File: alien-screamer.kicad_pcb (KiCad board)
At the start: 2 copper layers, 34 parts, among them Q2 2N3904, Q3 2N3904, SW1 S4

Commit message: commit
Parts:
- added X1-1: TestPoint, TestPoint:TestPoint_THTPad_D1.0mm_Drill0.5mm, F.Cu at (217.0, 65.5)
- added X13: TestPoint, TestPoint:TestPoint_THTPad_D1.0mm_Drill0.5mm, F.Cu at (166.9, 105.9)
- added X13-1: TestPoint, TestPoint:TestPoint_THTPad_D1.0mm_Drill0.5mm, F.Cu at (238.5, 70.5)
- added X14: TestPoint, TestPoint:TestPoint_THTPad_D1.0mm_Drill0.5mm, F.Cu at (166.9, 112.0)
- added X14-1: TestPoint, TestPoint:TestPoint_THTPad_D1.0mm_Drill0.5mm, F.Cu at (232.0, 69.5)
- added X2: TestPoint, TestPoint:TestPoint_THTPad_D1.0mm_Drill0.5mm, F.Cu at (204.5, 67.0)
- added X2-1: TestPoint, TestPoint:TestPoint_THTPad_D1.0mm_Drill0.5mm, F.Cu at (173.0, 105.9)
- added X3: TestPoint, TestPoint:TestPoint_THTPad_D1.0mm_Drill0.5mm, F.Cu at (224.0, 68.0)
- added X3-1: TestPoint, TestPoint:TestPoint_THTPad_D1.0mm_Drill0.5mm, F.Cu at (173.0, 112.0)
- added X4: TestPoint, TestPoint:TestPoint_THTPad_D1.0mm_Drill0.5mm, F.Cu at (160.8, 105.9)
- added X4-1: TestPoint, TestPoint:TestPoint_THTPad_D1.0mm_Drill0.5mm, F.Cu at (186.5, 66.5)
- added X5: TestPoint, TestPoint:TestPoint_THTPad_D1.0mm_Drill0.5mm, F.Cu at (160.8, 112.0)
- added X5-1: TestPoint, TestPoint:TestPoint_THTPad_D1.0mm_Drill0.5mm, F.Cu at (184.0, 66.5)
- added X6: TestPoint, TestPoint:TestPoint_THTPad_D1.0mm_Drill0.5mm, F.Cu at (221.0, 71.0)
- added X6-1: TestPoint, TestPoint:TestPoint_THTPad_D1.0mm_Drill0.5mm, F.Cu at (179.1, 99.8)
- added X7: TestPoint, TestPoint:TestPoint_THTPad_D1.0mm_Drill0.5mm, F.Cu at (166.9, 93.7)
- added X7-1: TestPoint, TestPoint:TestPoint_THTPad_D1.0mm_Drill0.5mm, F.Cu at (179.1, 105.9)
- added X8: TestPoint, TestPoint:TestPoint_THTPad_D1.0mm_Drill0.5mm, F.Cu at (166.9, 99.8)
- added X9-1: TestPoint, TestPoint:TestPoint_THTPad_D1.0mm_Drill0.5mm, F.Cu at (179.1, 112.0)
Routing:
- net Net-(R4-Pad2): track 0.00 -> 19.8 mm, vias 0 -> 1
- net Net-(C12-Pad1): track 0.00 -> 18.0 mm
- net Net-(Q1-S): track 0.40 -> 17.9 mm
- net Net-(R6-Pad2): track 0.00 -> 14.3 mm
- net Net-(R10-Pad1): track 0.00 -> 13.8 mm
- net Net-(S3-B): track 0.00 -> 10.9 mm
- net Net-(S1-A): track 23.6 -> 31.2 mm
- net Net-(S2-A): track 0.50 -> 8.00 mm

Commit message: commit
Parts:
- added B1: TestPoint_2Pole, TestPoint:TestPoint_2Pads_Pitch5.08mm_Drill1.3mm, F.Cu at (201.6, 104.8)
- added C1: 100p, TestPoint:TestPoint_2Pads_Pitch5.08mm_Drill1.3mm, F.Cu at (201.6, 109.4)
- added C10: 220u, Capacitor_THT:CP_Radial_D10.0mm_P5.00mm, F.Cu at (76.5, 102.0)
- added C11: .1u, Capacitor_THT:C_Disc_D7.5mm_W5.0mm_P5.00mm, F.Cu at (56.9, 107.6)
- added C12: 1u, Capacitor_THT:C_Disc_D7.5mm_W5.0mm_P5.00mm, F.Cu at (65.9, 88.0)
- added C13: .047u, Capacitor_THT:C_Disc_D7.5mm_W5.0mm_P5.00mm, F.Cu at (65.9, 94.5)
- added C14: 10u, Capacitor_THT:C_Disc_D7.5mm_W5.0mm_P5.00mm, F.Cu at (65.9, 101.0)
- added C2: 1u, Capacitor_THT:C_Disc_D7.5mm_W5.0mm_P5.00mm, F.Cu at (47.8, 88.0)
- added C3: .001u, Capacitor_THT:C_Disc_D7.5mm_W5.0mm_P5.00mm, F.Cu at (47.8, 94.5)
- added C4: 1u, Capacitor_THT:C_Disc_D7.5mm_W5.0mm_P5.00mm, F.Cu at (47.8, 101.0)
- added C5: 1u, Capacitor_THT:C_Disc_D7.5mm_W5.0mm_P5.00mm, F.Cu at (47.8, 107.6)
- added C6: .01u, Capacitor_THT:C_Disc_D7.5mm_W5.0mm_P5.00mm, F.Cu at (56.9, 88.0)
- added C7: .1u, Capacitor_THT:C_Disc_D7.5mm_W5.0mm_P5.00mm, F.Cu at (56.9, 94.5)
- added C8: 470u, Capacitor_THT:CP_Radial_D10.0mm_P5.00mm, F.Cu at (76.5, 90.5)
- added C9: .1u, Capacitor_THT:C_Disc_D7.5mm_W5.0mm_P5.00mm, F.Cu at (56.9, 101.0)
- added D1: D, Diode_THT:D_DO-15_P10.16mm_Horizontal, F.Cu at (201.2, 99.9)
- added J1: AudioJack2, TestPoint:TestPoint_2Pads_Pitch5.08mm_Drill1.3mm, F.Cu at (201.6, 114.1)
- added LFO1: LED1, LED_THT:LED_D5.0mm, F.Cu at (211.4, 106.2)
- added Q1: 2N5457, Package_TO_SOT_THT:TO-92_HandSolder, F.Cu at (211.0, 113.5)
- added TP1: TestPoint_2Pole, TestPoint:TestPoint_2Pads_Pitch5.08mm_Drill1.3mm, F.Cu at (59.7, 124.9)
- added U1: LM324, Package_DIP:DIP-14_W7.62mm_LongPads, F.Cu at (47.8, 112.9)
- added U2: LM386, Package_DIP:DIP-8_W7.62mm_LongPads, F.Cu at (59.4, 112.9)
- added X1: TestPoint, TestPoint:TestPoint_THTPad_D1.0mm_Drill0.5mm, F.Cu at (214.9, 98.8)

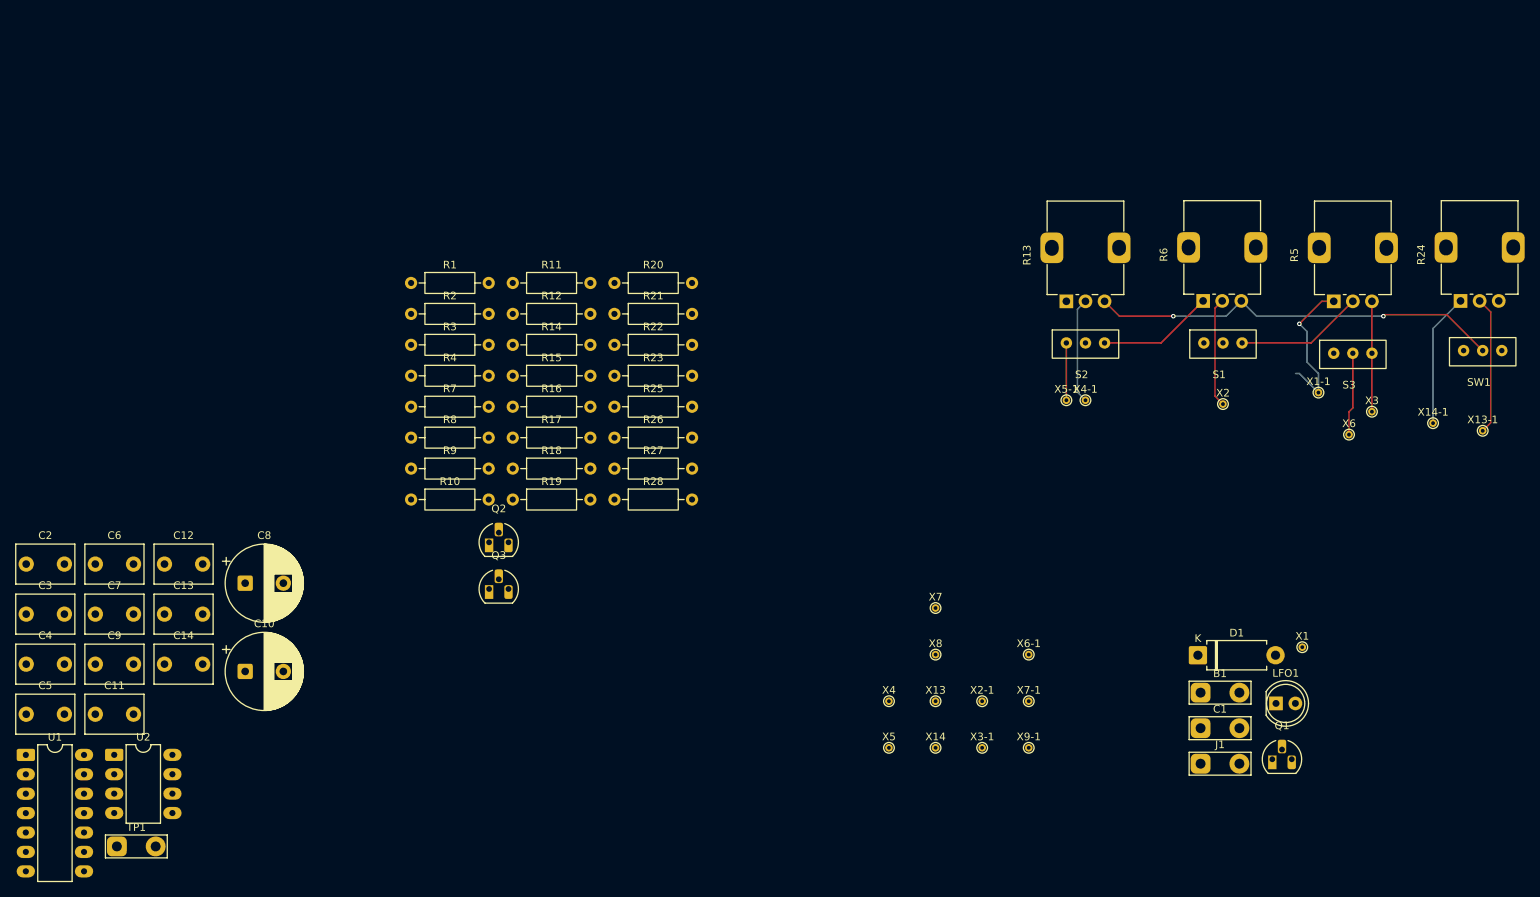
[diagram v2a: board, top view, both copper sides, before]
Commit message: Finished PCB, experimenting with connectors - unsure if it will work but have sent off PCB design for fabrication
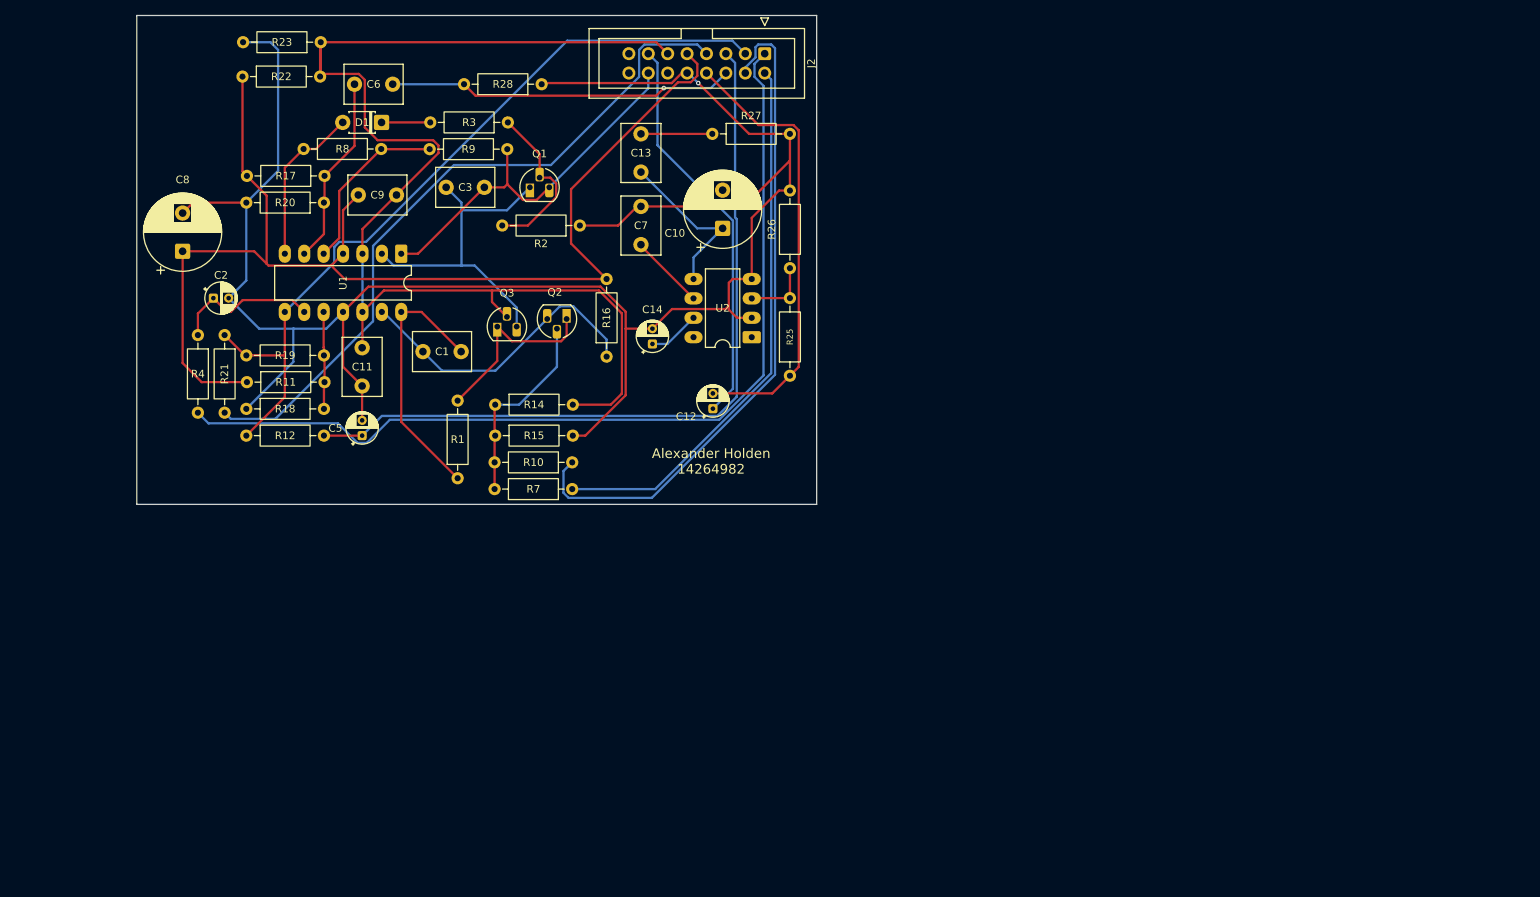
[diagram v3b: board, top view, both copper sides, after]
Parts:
- removed B1, TP1: TestPoint_2Pole, TestPoint:TestPoint_2Pads_Pitch5.08mm_Drill1.3mm
- removed C4: 1u, Capacitor_THT:C_Disc_D7.5mm_W5.0mm_P5.00mm
- removed J1: AudioJack2, TestPoint:TestPoint_2Pads_Pitch5.08mm_Drill1.3mm
- removed LFO1: LED1, LED_THT:LED_D5.0mm
- removed R13, R24, R6: 100K, Potentiometer_THT:Potentiometer_Alps_RK09K_Single_Vertical
- removed R5: 1M, Potentiometer_THT:Potentiometer_Alps_RK09K_Single_Vertical
- removed S1: SW_SPST, PROJECT_FOOTPRINTS:spdt
- removed S2: SW_SPDT_312, PROJECT_FOOTPRINTS:spdt
- removed S3: SYNC, PROJECT_FOOTPRINTS:spdt
- removed SW1: S4, PROJECT_FOOTPRINTS:spdt
- removed X1, X1-1, X13, X13-1, X14, X14-1, X2, X2-1, X3, X3-1, X4, X4-1, X5, X5-1, X6, X6-1, X7, X7-1, X8, X9-1: TestPoint, TestPoint:TestPoint_THTPad_D1.0mm_Drill0.5mm
- added J2: Conn_02x08_Odd_Even, PROJECT_FOOTPRINTS:IDC-Header_2x08_P2.54mm_Vertical, F.Cu at (144.5, 21.1)
- C1: footprint TestPoint:TestPoint_2Pads_Pitch5.08mm_Drill1.3mm -> Capacitor_THT:C_Disc_D7.5mm_W5.0mm_P5.00mm
- C12, C14, C2, C5: footprint Capacitor_THT:C_Disc_D7.5mm_W5.0mm_P5.00mm -> Capacitor_THT:CP_Radial_D4.0mm_P2.00mm
- D1: footprint Diode_THT:D_DO-15_P10.16mm_Horizontal -> Diode_THT:D_T-1_P5.08mm_Horizontal
- moved D1 127.6 mm to (94.3, 30.1), turned to 180 degrees
- moved Q1 122.7 mm to (113.8, 38.6)
- moved C1 113.1 mm to (99.8, 60.1)
- moved U2 99.8 mm to (142.8, 58.3), turned to 180 degrees
- moved C7 86.3 mm to (128.3, 46.1), turned to 90 degrees
- moved C10 85.3 mm to (139.0, 44.0), turned to 90 degrees
- moved C13 85.1 mm to (128.3, 36.6), turned to 90 degrees
- moved U1 82.0 mm to (96.9, 47.3), turned to -90 degrees
- moved C3 78.4 mm to (102.8, 38.6)
- moved C14 76.4 mm to (129.8, 59.1), turned to 90 degrees
- moved C12 74.6 mm to (137.7, 67.6), turned to 90 degrees
- moved C6 73.9 mm to (95.8, 25.1), turned to 180 degrees
- moved C9 70.4 mm to (91.3, 39.6)
- moved R22 60.0 mm to (76.2, 24.1)
- moved C11 59.3 mm to (91.8, 59.6), turned to -90 degrees
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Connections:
- net Net-(C12-Pad2) renamed /X8
- net Net-(Q1-S) renamed /X14
- net Net-(S1-A) renamed /X3
- net Net-(S2-A) renamed /X5
- net Net-(S3-B) renamed /X6
- C12 pad 1: Net-(C12-Pad1) -> /X13
- R10 pad 1: Net-(R10-Pad1) -> /X4
- R21 pad 2: Net-(LFO1-A) -> /X7
- R4 pad 2: Net-(R4-Pad2) -> /X1
- R7 pad 1: Net-(R6-Pad2) -> /X2
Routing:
- net /BN: track 0.00 -> 268.9 mm, vias 0 -> 1
- net GND: track 0.00 -> 167.0 mm
- net /X1: track 0.00 -> 122.5 mm
- net /BP: track 54.0 -> 157.4 mm, vias 2 -> 0
- net /X5: track 8.00 -> 101.6 mm
- net /X7: track 0.00 -> 92.1 mm
- net /X4: track 0.00 -> 88.7 mm
- net /X3: track 31.2 -> 104.1 mm
- net /X2: track 0.00 -> 72.0 mm
- net /X8: track 0.00 -> 58.8 mm
- net /X13: track 0.00 -> 52.1 mm
- net Net-(Q1-D): track 0.00 -> 44.3 mm
- net Net-(Q2-C): track 0.00 -> 40.1 mm
- net Net-(C1-Pad2): track 0.00 -> 34.8 mm
- net /X6: track 10.9 -> 45.5 mm, vias 0 -> 1
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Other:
- board outline added: 89 x 64 mm
- board text added: "Alexander Holden 14264982"
